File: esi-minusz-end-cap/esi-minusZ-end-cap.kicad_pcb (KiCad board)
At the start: 4 copper layers, 105.6 x 105.6 mm, 44 parts, among them J1 M55-7011242R, J2 U.FL-R-SMA

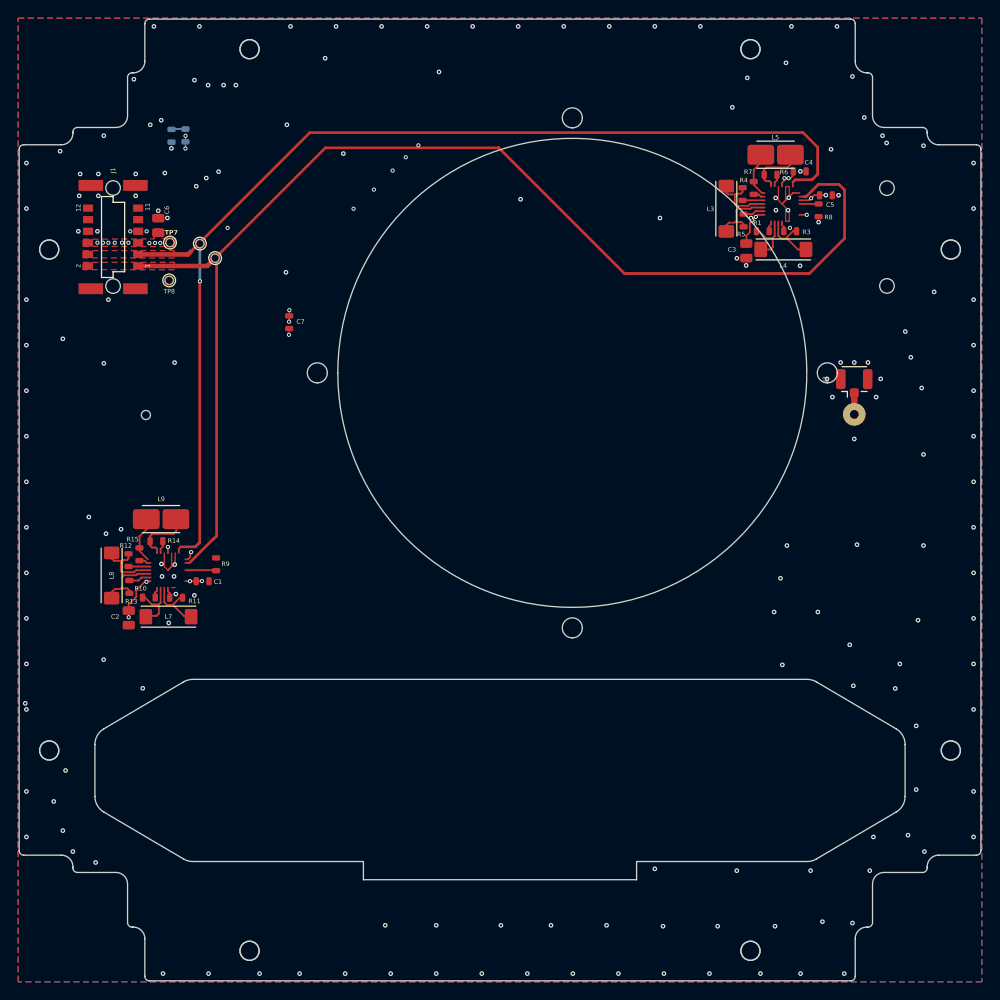
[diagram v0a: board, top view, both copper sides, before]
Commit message: New DFX & reposition GPS 7 magnetometers
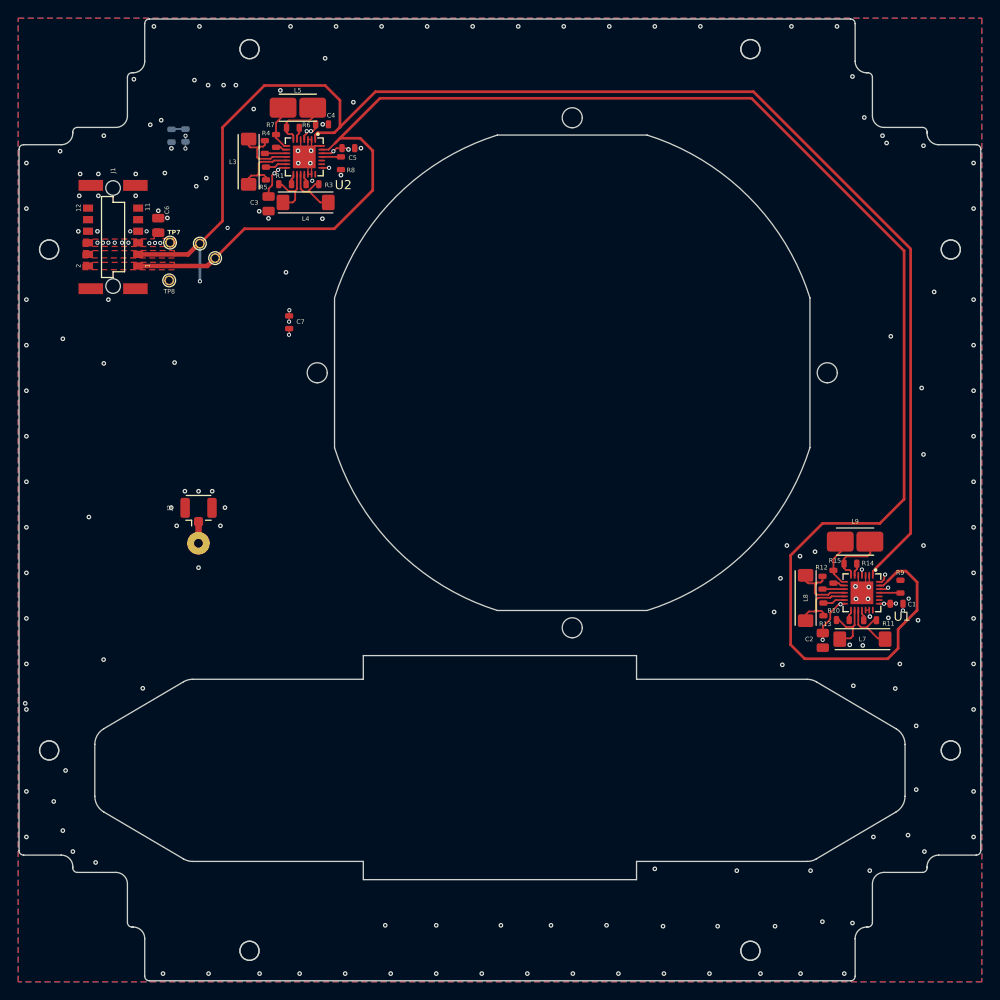
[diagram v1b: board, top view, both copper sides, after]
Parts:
- added U1: RM3100, oresat-misc:RM3100-MagI2C, F.Cu at (188.2, 115.2)
- added U2: RM3100, oresat-misc:RM3100-MagI2C, F.Cu at (127.0, 67.3)
- moved C1 76.2 mm to (192.1, 116.4)
- moved L7 76.2 mm to (188.3, 120.3)
- moved L9 76.2 mm to (187.5, 109.6)
- moved C2 76.2 mm to (183.9, 120.4)
- moved L8 76.2 mm to (182.1, 115.8)
- moved R10 76.2 mm to (186.1, 118.2)
- moved R12 76.2 mm to (183.9, 114.1)
- moved R11 76.2 mm to (189.1, 118.2)
- moved R13 76.2 mm to (184.0, 117.0)
- moved R14 76.2 mm to (187.0, 112.0)
- moved R15 76.2 mm to (185.1, 113.4)
- moved R9 75.2 mm to (192.5, 114.5)
- moved ANT1 73.4 mm to (115.4, 107.2)
- moved J2 73.4 mm to (115.4, 106.3)
- moved L4 52.7 mm to (127.2, 72.3)
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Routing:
- net /MAG-SDA: track 136.9 -> 189.6 mm
- net /MAG-SCL: track 123.7 -> 156.2 mm
- net +3.3v: track 22.6 -> 23.8 mm, vias 26 -> 27
- net Net-(U1-REXT): track 3.46 -> 2.33 mm
- net GND: vias 185 -> 171
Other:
- outline, holes or cut-outs redrawn

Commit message: New DFX (bias left) & rerouted accordingly. Made pretty. Done?
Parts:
- moved ANT1 68.5 mm to (182.5, 93.2)
- moved J2 68.5 mm to (182.5, 92.3)
- moved C4 50.1 mm to (113.6, 111.5)
- moved C3 49.9 mm to (107.6, 120.0)
- moved R6 49.9 mm to (110.3, 111.6)
- moved U2 49.9 mm to (111.6, 114.8)
- moved L5 49.9 mm to (110.9, 109.4)
- moved C5 49.9 mm to (116.4, 113.9)
- moved L3 49.9 mm to (105.5, 115.4)
- moved L4 49.9 mm to (111.7, 119.8)
- moved R1 49.9 mm to (109.5, 117.8)
- moved R3 49.9 mm to (112.5, 117.8)
- moved R4 49.9 mm to (107.2, 113.7)
- moved R5 49.9 mm to (107.4, 116.6)
- moved R7 49.9 mm to (108.5, 113.1)
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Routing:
- net /MAG-SDA: track 189.6 -> 141.6 mm
- net /MAG-SCL: track 156.2 -> 133.4 mm, vias 1 -> 0
- net GND: vias 171 -> 195
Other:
- outline, holes or cut-outs redrawn
- board text added: "3.3v"
- board text added: "GND"
- board text added: "MAG-SCL"
- board text added: "MAG-SDA"

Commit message: ESI -Z end cap, with build files, final answer
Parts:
- moved J2 0.47 mm to (182.5, 91.8)
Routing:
- net GND: vias 195 -> 203
